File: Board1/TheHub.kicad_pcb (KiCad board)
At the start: 2 copper layers, 118.7 x 184.1 mm, 51 parts, among them J11 RFD900, J12 I2C_1 Test Point, J13 I2C_2 Test Point, J15 GPIO Test, J16 I2C_3 Test Point, J17 12V OUT, J23 NucleoRight, J5 NucleoLeft, J8 12V MAIN POWER, U10 ADXL377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

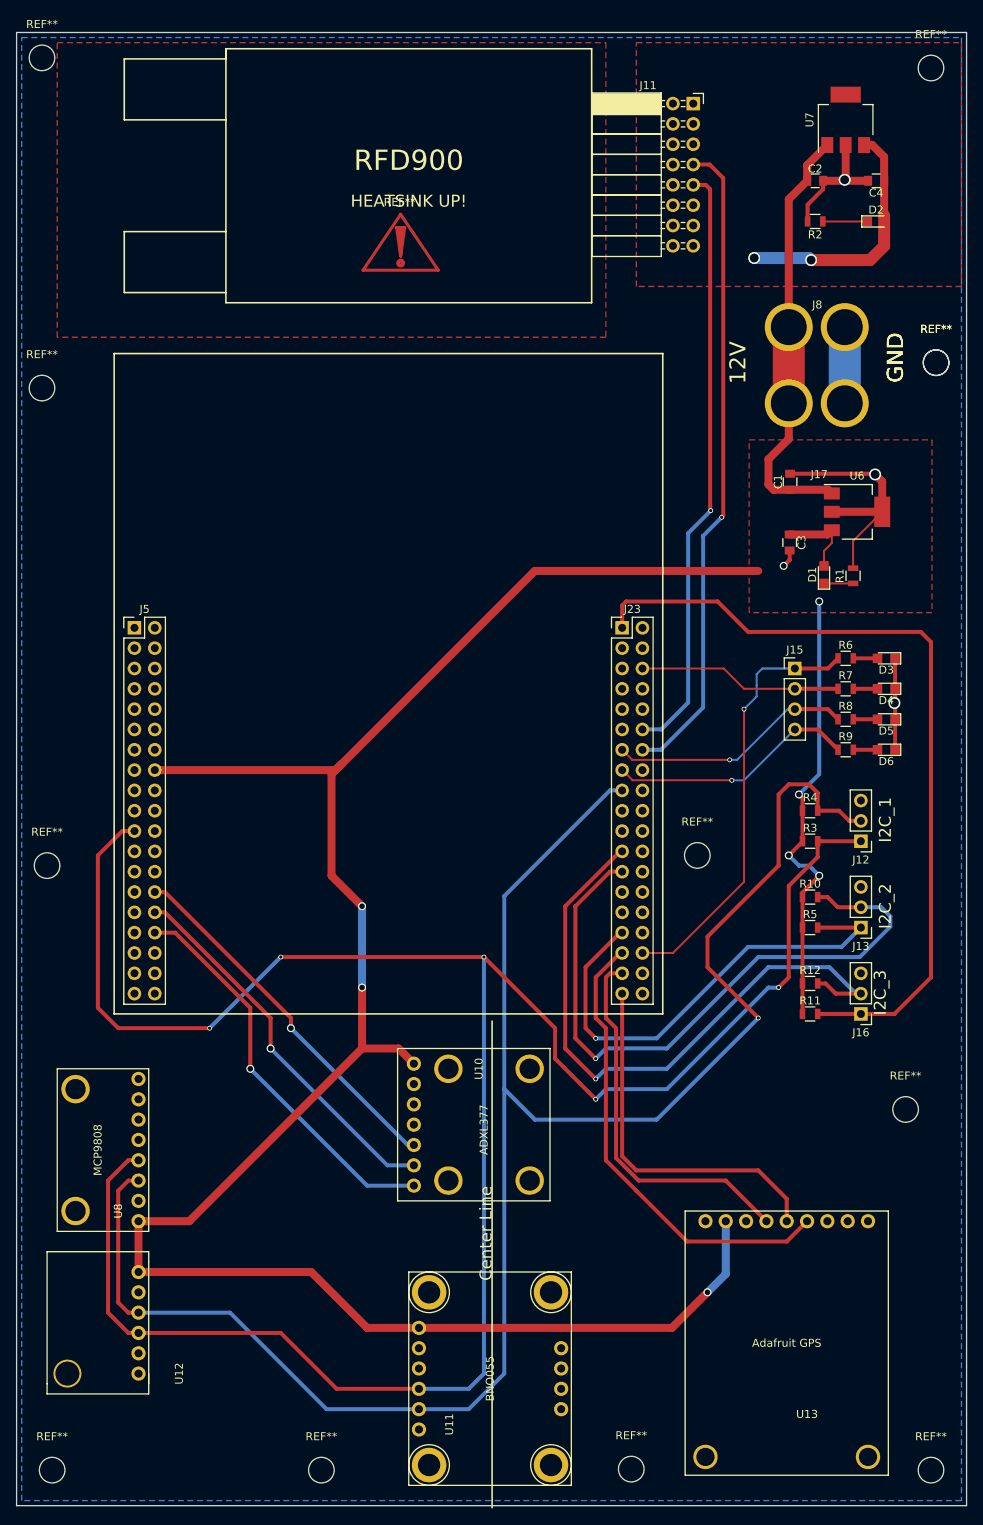
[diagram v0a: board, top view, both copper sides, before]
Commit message: Align hole mounts
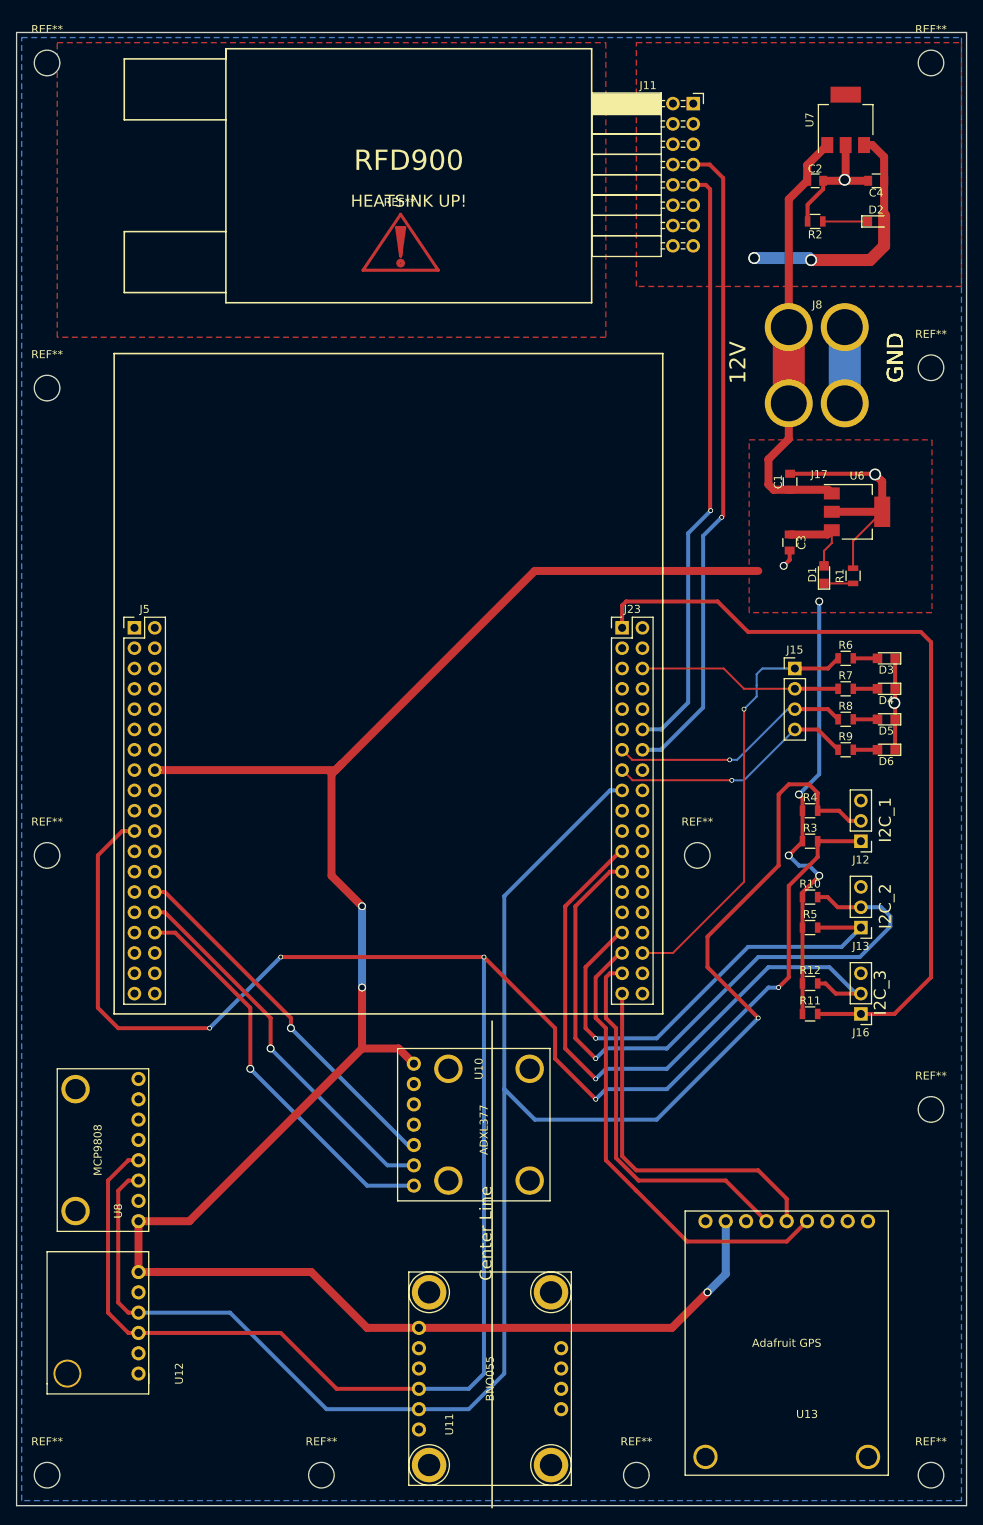
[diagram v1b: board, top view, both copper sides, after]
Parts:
- removed the REF** at (177.2, 92.1)
- moved REF** 3.18 mm to (176.5, 185.4)
- moved REF** 1.27 mm to (66.0, 153.7)
- moved REF** 0.99 mm to (139.7, 231.1)
- moved REF** 0.90 mm to (66.0, 54.6)
- moved REF** 0.90 mm to (176.5, 92.7)
- moved REF** 0.90 mm to (66.0, 231.1)
- moved REF** 0.64 mm to (66.0, 95.2)
- moved REF** 0.63 mm to (176.5, 54.6)
- moved REF** 0.63 mm to (100.3, 231.1)
- moved REF** 0.63 mm to (176.5, 231.1)
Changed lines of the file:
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@@
     (tracks 318)
     (zones 0)
-    (modules 51)
+    (modules 50)
     (nets 107)
   )
@@
   )
   (module Mounting_Holes:MountingHole_3.2mm_M3 (layer F.Cu)
-    (at 177.165 92.075)
+    (at 176.53 92.71)
     (descr "Mounting Hole 3.2mm, no annular, M3")
     (tags "mounting hole 3.2mm no annular m3")
@@
   )
   (module Mounting_Holes:MountingHole_3.2mm_M3 (layer F.Cu)
-    (at 66.675 230.505)
+    (at 66.04 231.14)
     (descr "Mounting Hole 3.2mm, no annular, M3")
     (tags "mounting hole 3.2mm no annular m3")
@@
   )
   (module Mounting_Holes:MountingHole_3.2mm_M3 (layer F.Cu)
-    (at 176.53 230.505)
+    (at 176.53 231.14)
     (descr "Mounting Hole 3.2mm, no annular, M3")
     (tags "mounting hole 3.2mm no annular m3")
@@
   )
   (module Mounting_Holes:MountingHole_3.2mm_M3 (layer F.Cu)
-    (at 65.405 53.975)
+    (at 66.04 54.61)
     (descr "Mounting Hole 3.2mm, no annular, M3")
     (tags "mounting hole 3.2mm no annular m3")
@@
   )
   (module Mounting_Holes:MountingHole_3.2mm_M3 (layer F.Cu)
-    (at 65.405 95.25)
+    (at 66.04 95.25)
     (descr "Mounting Hole 3.2mm, no annular, M3")
     (tags "mounting hole 3.2mm no annular m3")
@@
   )
   (module Mounting_Holes:MountingHole_3.2mm_M3 (layer F.Cu)
-    (at 66.04 154.94)
+    (at 66.04 153.67)
     (descr "Mounting Hole 3.2mm, no annular, M3")
     (tags "mounting hole 3.2mm no annular m3")
@@
   )
   (module Mounting_Holes:MountingHole_3.2mm_M3 (layer F.Cu)
-    (at 177.165 92.075)
-    (descr "Mounting Hole 3.2mm, no annular, M3")
-    (tags "mounting hole 3.2mm no annular m3")
-    (fp_text reference REF** (at 0 -4.2) (layer F.SilkS)
-      (effects (font (size 1 1) (thickness 0.15)))
-    )
-    (fp_text value MountingHole_3.2mm_M3 (at 0 4.2) (layer F.Fab)
-      (effects (font (size 1 1) (thickness 0.15)))
-    )
-    (fp_circle (center 0 0) (end 3.2 0) (layer Cmts.User) (width 0.15))
-    (fp_circle (center 0 0) (end 3.45 0) (layer F.CrtYd) (width 0.05))
-    (pad 1 np_thru_hole circle (at 0 0) (size 3.2 3.2) (drill 3.2) (layers *.Cu *.Mask))
-  )
-  (module Mounting_Holes:MountingHole_3.2mm_M3 (layer F.Cu)
-    (at 173.355 185.42)
+    (at 176.53 185.42)
     (descr "Mounting Hole 3.2mm, no annular, M3")
     (tags "mounting hole 3.2mm no annular m3")
@@
   )
   (module Mounting_Holes:MountingHole_3.2mm_M3 (layer F.Cu)
-    (at 176.53 55.245)
+    (at 176.53 54.61)
     (descr "Mounting Hole 3.2mm, no annular, M3")
     (tags "mounting hole 3.2mm no annular m3")
@@
   )
   (module Mounting_Holes:MountingHole_3.2mm_M3 (layer F.Cu)
-    (at 100.33 230.505)
+    (at 100.33 231.14)
     (descr "Mounting Hole 3.2mm, no annular, M3")
     (tags "mounting hole 3.2mm no annular m3")
@@
   )
   (module Mounting_Holes:MountingHole_3.2mm_M3 (layer F.Cu)
-    (at 139.065 230.378)
+    (at 139.7 231.14)
     (descr "Mounting Hole 3.2mm, no annular, M3")
     (tags "mounting hole 3.2mm no annular m3")

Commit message: Add logo to the board
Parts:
- added G***: LOGO, Board1:CycloneRocketryLogo, B.Cu at (121.9, 141.0)
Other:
- board text added: "The Hub, Rev. 1 Danny Mallek 1/8/2018"
- board text removed: "The Hub, Board Rev. 1 To Rapid Prototype Danny Mallek 6/9/2017"

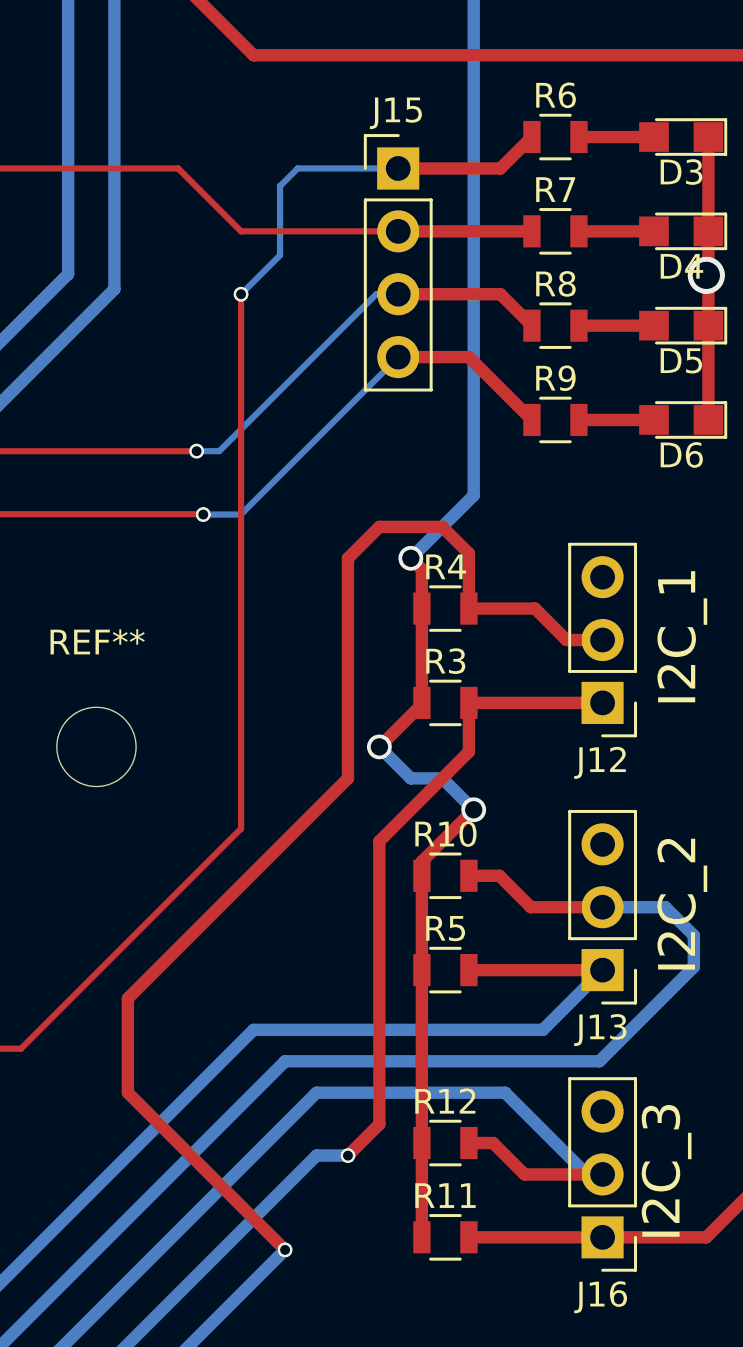
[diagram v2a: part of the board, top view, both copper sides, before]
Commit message: Add labeling text for probe points
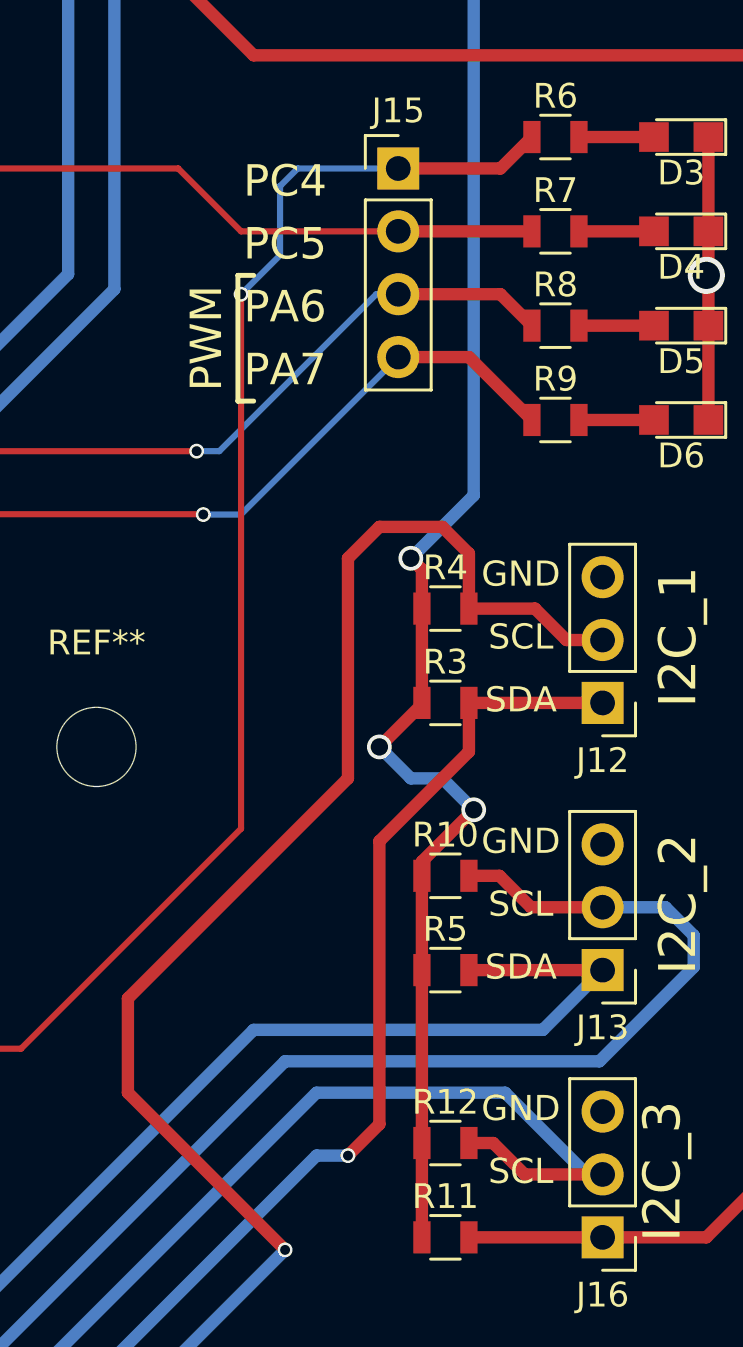
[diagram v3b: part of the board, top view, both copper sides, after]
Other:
- board text added: "PA6"
- board text added: "PA7"
- board text added: "PC4"
- board text added: "PC5"
- board text added: "PWM"
- board text added: "SCL"
- board text added: "SDA"
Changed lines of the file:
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@@
     (area 62.154999 50.724999 181.050001 235.025001)
     (thickness 1.6)
-    (drawings 33)
+    (drawings 49)
     (tracks 318)
     (zones 0)
@@
     (trace_clearance 0.2)
     (zone_clearance 0.508)
-    (zone_45_only no)
+    (zone_45_only yes)
     (trace_min 0.2)
     (segment_width 0.2)
@@
       (xy -15.895129 12.091526) (xy -15.76892 12.11999) (xy -15.549608 12.131504) (xy -15.333323 12.096166)) (layer B.SilkS) (width 0.01))
   )
+  (gr_text GND (at 164.465 168.275) (layer F.SilkS)
+    (effects (font (size 1.016 1.016) (thickness 0.254)))
+  )
+  (gr_text SCL (at 164.465 170.815) (layer F.SilkS)
+    (effects (font (size 1.016 1.016) (thickness 0.254)))
+  )
+  (gr_text GND (at 164.465 157.48) (layer F.SilkS)
+    (effects (font (size 1.016 1.016) (thickness 0.254)))
+  )
+  (gr_text SDA (at 164.465 162.56) (layer F.SilkS)
+    (effects (font (size 1.016 1.016) (thickness 0.254)))
+  )
+  (gr_text SCL (at 164.465 160.02) (layer F.SilkS)
+    (effects (font (size 1.016 1.016) (thickness 0.254)))
+  )
+  (gr_text SDA (at 164.465 151.765) (layer F.SilkS)
+    (effects (font (size 1.016 1.016) (thickness 0.254)))
+  )
+  (gr_text PWM (at 151.765 137.16 90) (layer F.SilkS)
+    (effects (font (size 1.27 1.27) (thickness 0.254)))
+  )
+  (gr_line (start 153.035 134.62) (end 153.67 134.62) (angle 90) (layer F.SilkS) (width 0.2))
+  (gr_line (start 153.035 139.7) (end 153.035 134.62) (angle 90) (layer F.SilkS) (width 0.2))
+  (gr_line (start 153.67 139.7) (end 153.035 139.7) (angle 90) (layer F.SilkS) (width 0.2))
+  (gr_text SCL (at 164.465 149.225) (layer F.SilkS)
+    (effects (font (size 1.016 1.016) (thickness 0.254)))
+  )
+  (gr_text GND (at 164.465 146.685) (layer F.SilkS)
+    (effects (font (size 1.016 1.016) (thickness 0.254)))
+  )
+  (gr_text PA7 (at 154.94 138.43) (layer F.SilkS)
+    (effects (font (size 1.27 1.27) (thickness 0.254)))
+  )
+  (gr_text PA6 (at 154.94 135.89) (layer F.SilkS)
+    (effects (font (size 1.27 1.27) (thickness 0.254)))
+  )
+  (gr_text PC5 (at 154.94 133.35) (layer F.SilkS)
+    (effects (font (size 1.27 1.27) (thickness 0.254)))
+  )
+  (gr_text PC4 (at 154.94 130.81) (layer F.SilkS)
+    (effects (font (size 1.27 1.27) (thickness 0.254)))
+  )
   (gr_text "Center Line" (at 120.904 200.914 90) (layer F.SilkS)
